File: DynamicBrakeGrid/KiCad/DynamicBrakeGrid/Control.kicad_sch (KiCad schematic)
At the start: 36 parts, among them IC5 LM358DR, IC6 MCP2515-e_ST, IC7 TJA1050T_CM,118, Y1 8MHz

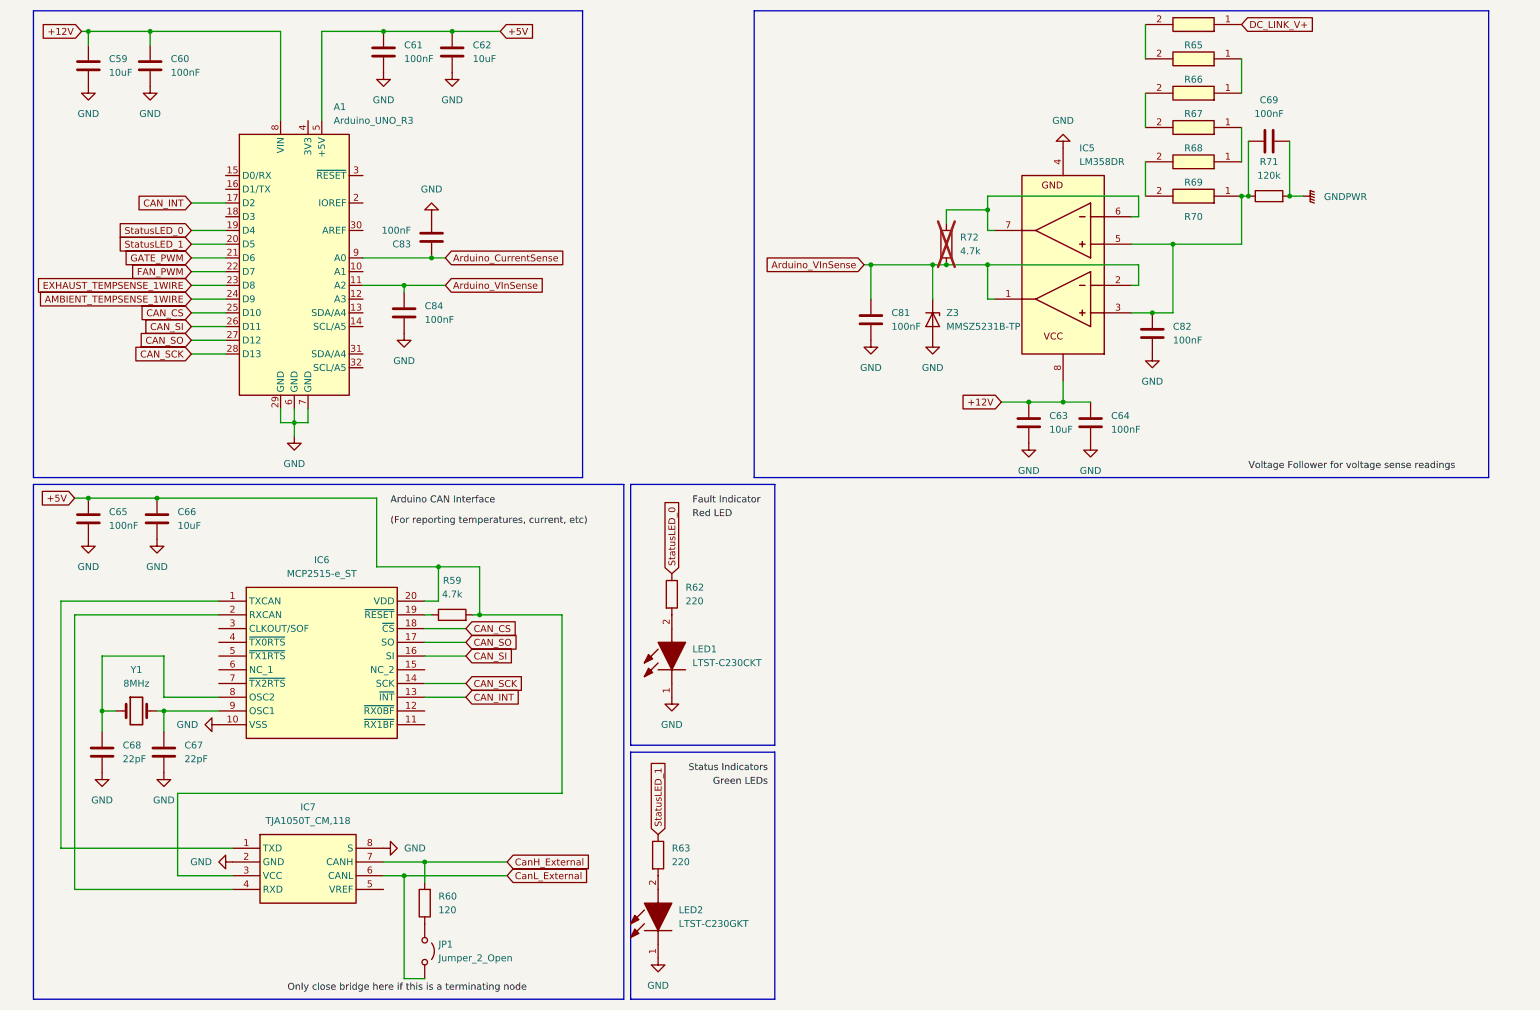
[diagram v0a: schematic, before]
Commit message: Update Schematics, Inverter, Gate Driver, Mechanical, Software
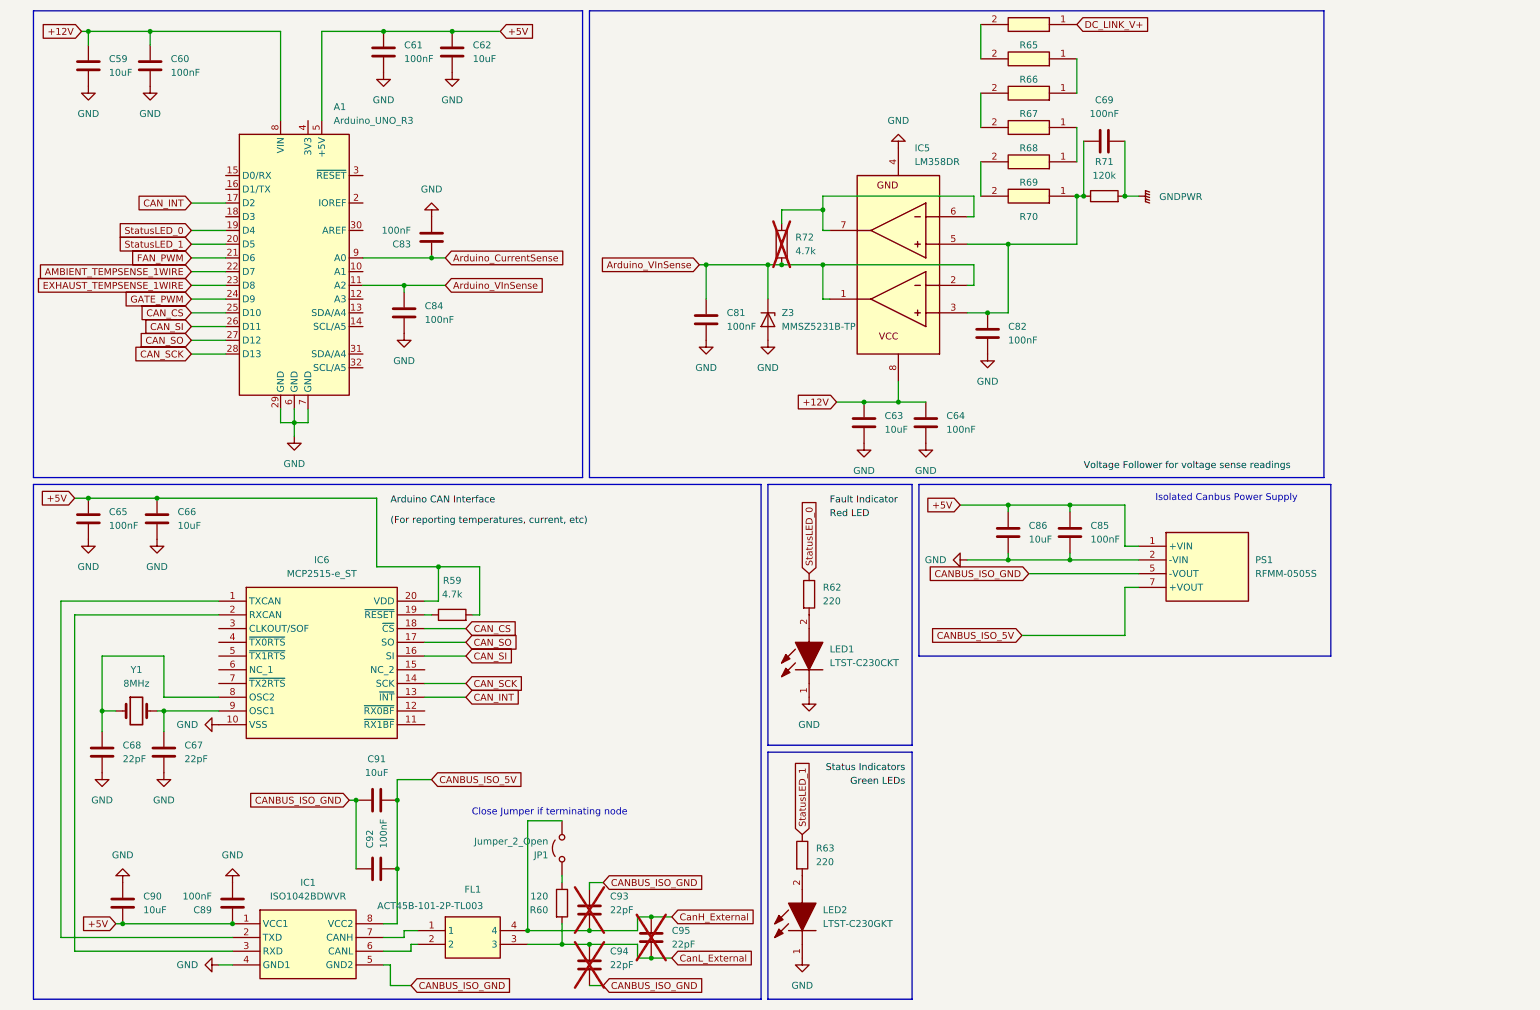
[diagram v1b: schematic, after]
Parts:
- removed IC7: TJA1050T_CM,118, InverterCom:SOIC127P600X175-8N, symbol InverterCom:TJA1050T_CM,118
- added C85, C89, C92: 100nF, Capacitor_SMD:C_1210_3225Metric_Pad1.33x2.70mm_HandSolder, symbol Device:C
- added C86, C90, C91: 10uF, Capacitor_SMD:C_1210_3225Metric_Pad1.33x2.70mm_HandSolder, symbol Device:C
- added C93, C94, C95: 22pF, Capacitor_SMD:C_1210_3225Metric_Pad1.33x2.70mm_HandSolder, symbol Device:C
- added FL1: ACT45B-101-2P-TL003, InverterCom:ACT45B1012PTL003, symbol InverterCom:ACT45B-101-2P-TL003
- added IC1: ISO1042BDWVR, InverterCom:SOIC127P1150X280-8N, symbol InverterCom:ISO1042BDWVR
- added PS1: RFMM-0505S, InverterCom:RFMM0505S, symbol InverterCom:RFMM-0505S
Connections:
- net +5V: now also C85.1, C86.1, C89.1, C90.2, IC1.1 (VCC1), PS1.1 (+VIN)
- net AMBIENT_TEMPSENSE_1WIRE: now also A1.22 (D7); no longer A1.24 (D9)
- net CanH_External: now also JP1.2 (B), C93.2, C95.1, FL1.4; no longer R60.2
- net CanL_External: now also R60.2, C94.1, C95.2, FL1.3; no longer JP1.2 (B)
- net FAN_PWM: now also A1.21 (D6); no longer A1.22 (D7)
- net GATE_PWM: now also A1.24 (D9); no longer A1.21 (D6)
- net GND: now also C85.2, C86.2, C89.2, C90.1, IC1.4 (GND1), PS1.2 (-VIN)
- net at IC6.1 (TXCAN): now also IC1.2 (TXD)
- net at IC6.2 (RXCAN): now also IC1.3 (RXD)
- new net: FL1.2, IC1.6 (CANL)
- new net: FL1.1, IC1.7 (CANH)
- new net CANBUS_ISO_5V: C91.1, C92.2, IC1.8 (VCC2), PS1.7 (+VOUT)
- new net CANBUS_ISO_GND: C91.2, C92.1, C93.1, C94.2, IC1.5 (GND2), PS1.5 (-VOUT)
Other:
- note added: "Close Jumper if terminating node"
- note added: "Isolated Canbus Power Supply"
- moved on the sheet: C63, C64, C69, C81, C82, IC5, JP1, LED1, LED2, R60, R62, R63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

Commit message: u
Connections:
- net FAN_PWM: now also A1.24 (D9); no longer A1.21 (D6)
- net GATE_PWM: now also A1.21 (D6); no longer A1.24 (D9)
